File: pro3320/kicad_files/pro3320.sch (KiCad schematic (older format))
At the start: 52 parts

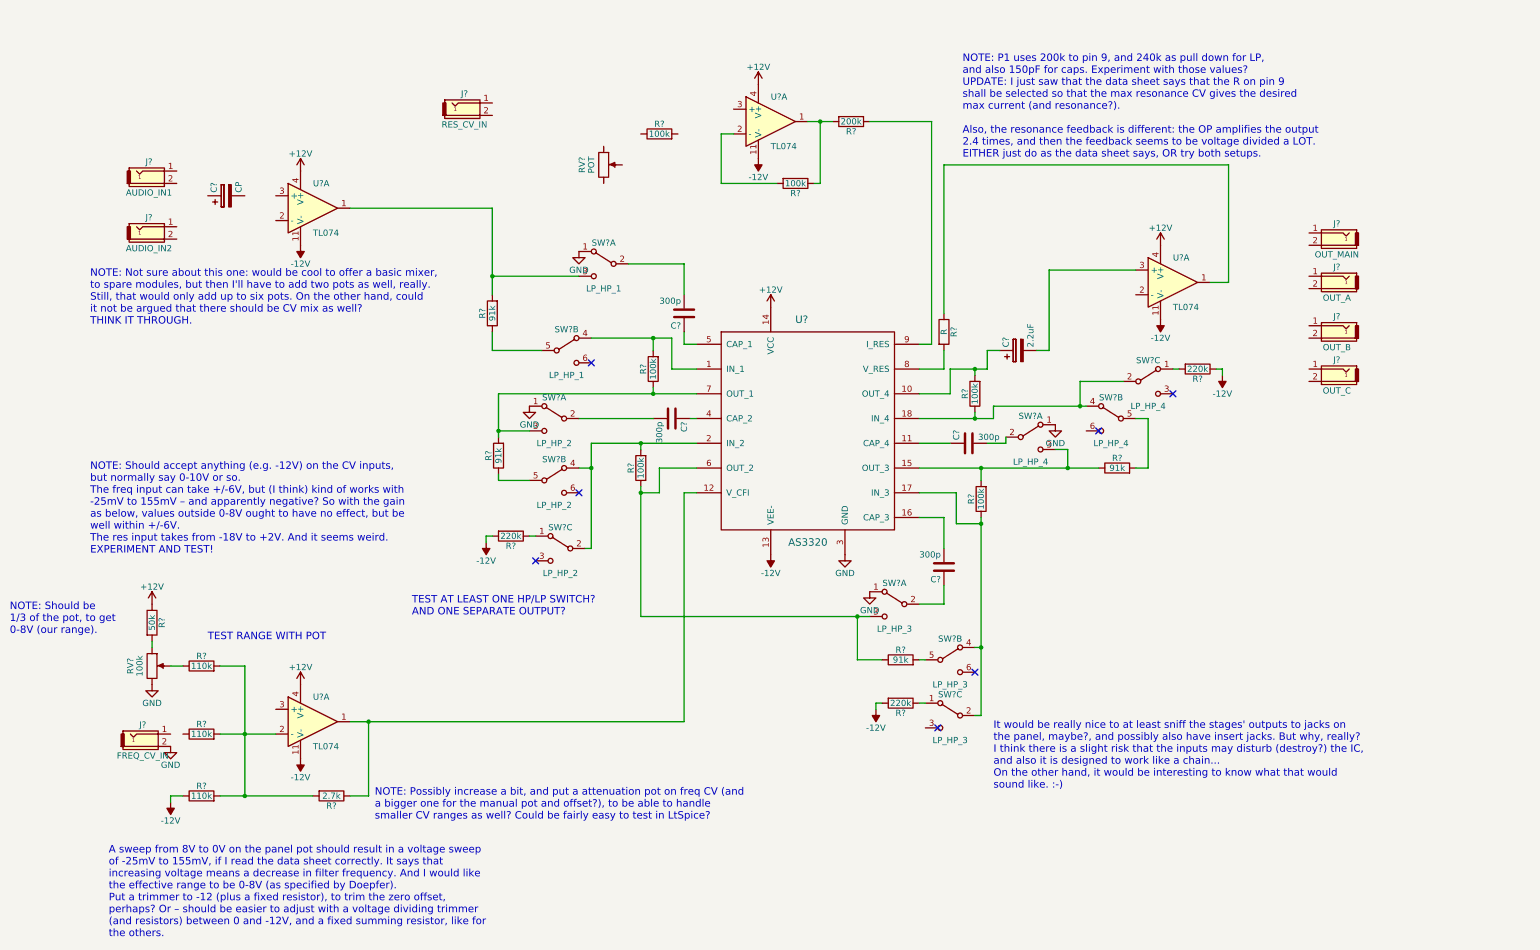
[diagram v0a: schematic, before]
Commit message: Finish (kind of) 3320 VCF
OK, it's not finished as such, nothing is tested at this point.
But the schematic is complete as far as I can tell without having
tested it. :-)
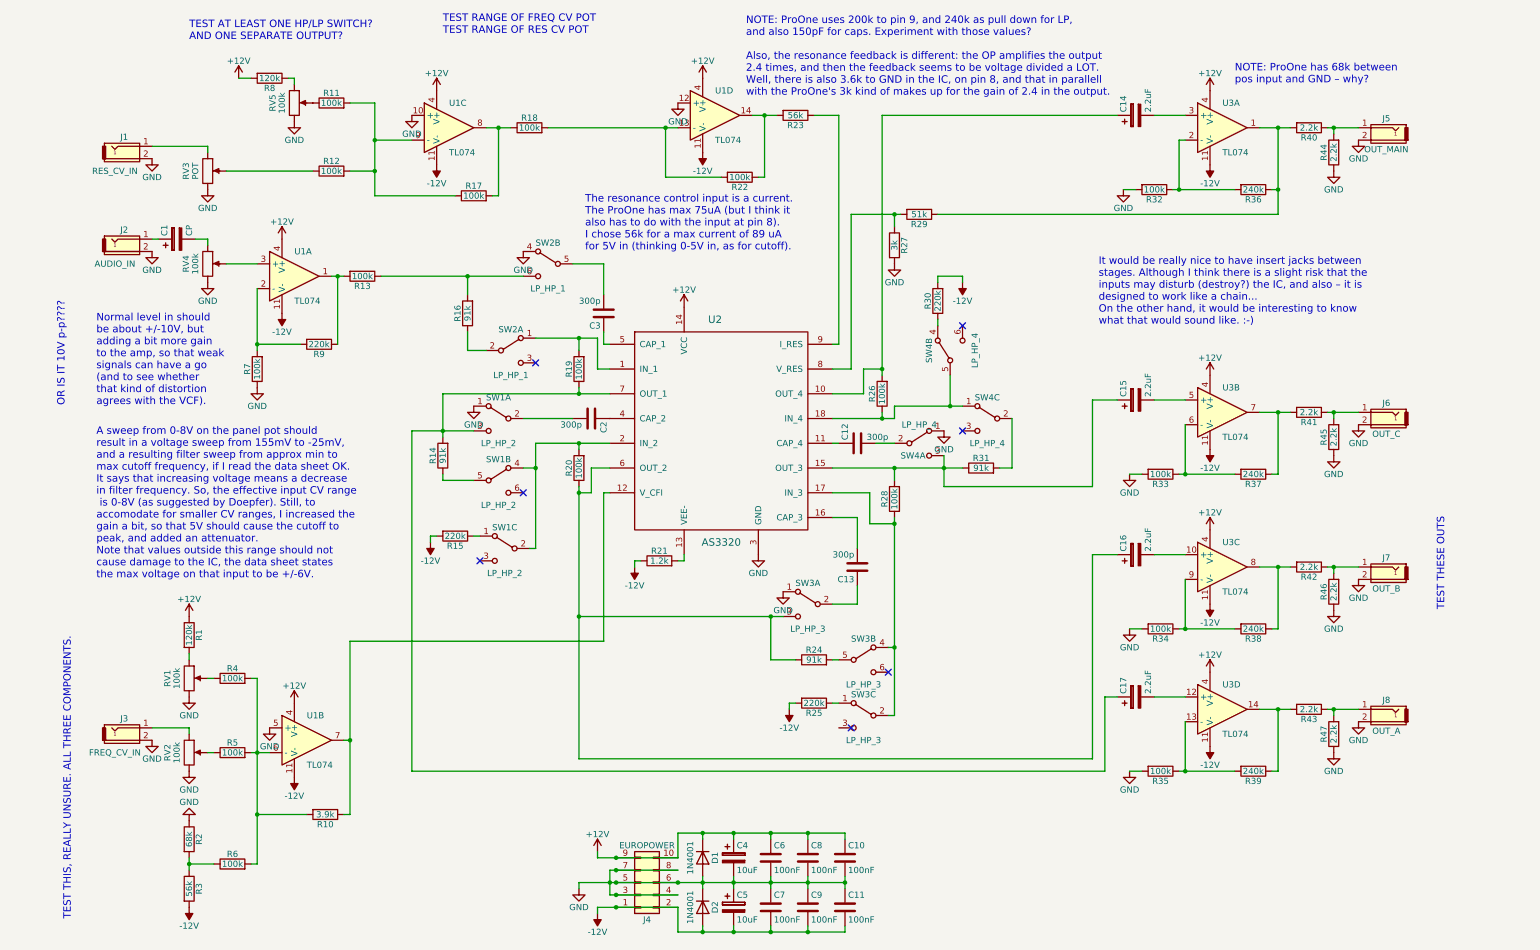
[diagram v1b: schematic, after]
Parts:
- removed J?: AUDIO_IN2, symbol Audio-Jack-2
- added C10, C11, C6, C7, C8, C9: 100nF, symbol C
- added C15, C16, C17: 2.2uF, symbol CP
- added C4, C5: 10uF, symbol CP
- added D1, D2: 1N4001, Diodes_THT:D_DO-41_SOD81_Horizontal_RM10, symbol 1N4001
- added J4: EUROPOWER, symbol Conn_02x05_Odd_Even
- added R11, R12, R13, R18, R32, R33, R34, R35, R7: 100k, symbol R
- added R2: 68k, symbol R
- added R21: 1.2k, symbol R
- added R27: 3k, symbol R
- added R3: 56k, symbol R
- added R36, R37, R38, R39: 240k, symbol R
- added R40, R41, R42, R43, R44, R45, R46, R47: 2.2k, symbol R
- added R8: 120k, symbol R
- added R9: 220k, symbol R
- added RV2, RV4, RV5: 100k, symbol POT
- added unit 3 of U1
- added unit 3 of U3
- added unit 4 of U3
- added unit 2 of U3
- J2: renamed from J?; value AUDIO_IN1 -> AUDIO_IN
- R1: renamed from R?; value 50k -> 120k
- R10: renamed from R?; value 2.7k -> 3.9k
- R23: renamed from R?; value 200k -> 56k
- R29: renamed from R?; value R -> 51k
- R4, R5, R6: renamed from R?; value 110k -> 100k
- gave numbers to parts that had none: 34
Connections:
- net +12V: now also C10.1, C4.1, C6.1, C8.1, D1.1 (K), J4.10 (Pin_10), J4.9 (Pin_9), R8.2, U1.4 (V+), U3.4 (V+), U3.4 (V+), U3.4 (V+)
- net -12V: now also R30.2, C11.2, C5.2, C7.2, C9.2, D2.2 (A), J4.1 (Pin_1), J4.2 (Pin_2), R21.1, R3.2, U1.11 (V-), U3.11 (V-), U3.11 (V-), U3.11 (V-); no longer R30.1, R6.1, U2.13 (VEE-)
- net GND: now also J1.2, J2.2, J5.2, J6.2, J7.2, J8.2, RV3.3, SW2.4 (A), U1.12 (+), U1.5 (+), C10.2, C11.1, C4.2, C5.1, C6.2, C7.1, C8.2, C9.1, D1.2 (A), D2.1 (K), J4.3 (Pin_3), J4.4 (Pin_4), J4.5 (Pin_5), J4.6 (Pin_6), J4.7 (Pin_7), J4.8 (Pin_8), R2.1, R27.2, R32.2, R33.2, R34.2, R35.2, R44.1, R45.1, R46.1, R47.1, R7.1, RV2.3, RV4.3, RV5.3, U1.10 (+); no longer SW2.1 (A)
- net at R19.2, U2.1 (IN_1): now also SW2.1 (A); no longer SW2.4 (A)
- net at R10.1, U2.12 (V_CFI): now also U1.7; no longer U1.1
- net at R28.2, R31.1, SW4.3 (C)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: now also C15.1
- net at R26.1, U2.18 (IN_4): now also SW4.1 (A), SW4.5 (B); no longer SW4.2 (B), SW4.4 (A)
- net at R20.1, R24.1, SW3.3 (C)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: now also C16.1
- net at R14.2, R19.1, SW1.3 (C)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: now also C17.1
- net at R29.2, U2.8 (V_RES): now also R27.1
- net at J3.1: now also RV2.1
- net at J1.1: now also RV3.1
- net at U1.2 (-): now also R7.2, R9.2
- net at U1.3 (+): now also RV4.2
- net at R10.2, R4.2, R5.2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: now also U1.6 (-); no longer U1.2 (-)
- net at R22.1, R23.2: now also U1.14; no longer U1.1
- net at R22.2: now also U1.13 (-), R18.2; no longer U1.2 (-)
- net at R29.1, U3.1: now also R36.1, R40.2
- net at U3.2 (-): now also R32.1, R36.2
- net at J2.1: now also C1.1
- net at C3.2: now also SW2.5 (B); no longer SW2.2 (B)
- net at R16.1: now also SW2.2 (B); no longer SW2.5 (B)
- net at C1.2: now also RV4.1
- net at R31.2: now also SW4.2 (B); no longer SW4.5 (B)
- net at R17.1: now also R11.2, R12.2, U1.9 (-)
- net at R17.2: now also R18.1, U1.8
- net at RV3.2: now also R12.1
- net at R5.1: now also RV2.2
- net at J5.1: now also R40.1, R44.2
- net at J8.1: now also R43.1, R47.2
- net at J7.1: now also R42.1, R46.2
- net at J6.1: now also R41.1, R45.2
- new net: R21.2, U2.13 (VEE-)
- new net: R13.2, R9.1, U1.1
- new net: R13.1, R16.2, SW2.6 (C)
- new net: R30.1, SW4.4 (A)
- new net: R2.2, R3.1, R6.1
- new net: C16.2, U3.10 (+)
- new net: R38.1, R42.2, U3.8
- new net: R34.1, R38.2, U3.9 (-)
- new net: C17.2, U3.12 (+)
- new net: R35.1, R39.2, U3.13 (-)
- new net: R39.1, R43.2, U3.14
- new net: C15.2, U3.5 (+)
- new net: R33.1, R37.2, U3.6 (-)
- new net: R37.1, R41.2, U3.7
- new net: R8.1, RV5.1
- new net: R11.1, RV5.2
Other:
- note added: "A sweep from 0-8V on the panel pot should \nresult in a voltage sweep from 155mV to -25mV, \nand a resulting filter sweep from approx min to \nmax cutoff frequency, if I read the data sheet OK. \nIt says that increasing voltage means a decrease \nin filter frequency. So, the effective input CV range\n is 0-8V (as suggested by Doepfer). Still, to \naccomodate for smaller CV ranges, I increased the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"
- note added: "It would be really nice to have insert jacks between \nstages. Although I think there is a slight risk that the \ninputs may disturb (destroy?) the IC, and also – it is \ndesigned to work like a chain... \nOn the other hand, it would be interesting to know \nwhat that would sound like. :-)"
- note added: "NOTE: ProOne has 68k between \npos input and GND – why?\n"
- note added: "NOTE: ProOne uses 200k to pin 9, and 240k as pull down for LP, \nand also 150pF for caps. Experiment with those values? \n\nAlso, the resonance feedback is different: the OP amplifies the output \n2.4 times, and then the feedback seems to be voltage divided a LOT. \nWell, there is also 3.6k to GND in the IC, on pin 8, and that in parallell\nwith the ProOne's 3k kind of makes up for the gain of 2.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"
- note added: "Normal level in should \nbe about +/-10V, but \nadding a bit more gain \nto the amp, so that weak\nsignals can have a go \n(and to see whether \nthat kind of distortion \nagrees with the VCF)."
- note added: "OR IS IT 10V p-p????\n"
- note added: "TEST RANGE OF FREQ CV POT\nTEST RANGE OF RES CV POT\n"
- note added: "TEST THESE OUTS"
- note added: "TEST THIS, REALLY UNSURE. ALL THREE COMPONENTS."
- note added: "The resonance control input is a current.\nThe ProOne has max 75uA (but I think it\nalso has to do with the input at pin 8).\nI chose 56k for a max current of 89 uA\nfor 5V in (thinking 0-5V in, as for cutoff).\n"
- note removed: "A sweep from 8V to 0V on the panel pot should result in a voltage sweep \nof -25mV to 155mV, if I read the data sheet correctly. It says that \nincreasing voltage means a decrease in filter frequency. And I would like\nthe effective range to be 0-8V (as specified by Doepfer). \nPut a trimmer to -12 (plus a fixed resistor), to trim the zero offset, \nperhaps? Or – should be easier to adjust with a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"
- note removed: "It would be really nice to at least sniff the stages' outputs to jacks on \nthe panel, maybe?, and possibly also have insert jacks. But why, really? \nI think there is a slight risk that the inputs may disturb (destroy?) the IC,\nand also it is designed to work like a chain... \nOn the other hand, it would be interesting to know what that would \nsound like. :-)"
- note removed: "NOTE: Not sure about this one: would be cool to offer a basic mixer,\nto spare modules, but then I'll have to add two pots as well, really. \nStill, that would only add up to six pots. On the other hand, could\nit not be argued that there should be CV mix as well?\nTHINK IT THROUGH."
- note removed: "NOTE: P1 uses 200k to pin 9, and 240k as pull down for LP, \nand also 150pF for caps. Experiment with those values? \nUPDATE: I just saw that the data sheet says that the R on pin 9\nshall be selected so that the max resonance CV gives the desired \nmax current (and resonance?).\n\nAlso, the resonance feedback is different: the OP amplifies the output \n2.4 times, and then the feedback seems to b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"
- note removed: "NOTE: Possibly increase a bit, and put a attenuation pot on freq CV (and \na bigger one for the manual pot and offset?), to be able to handle \nsmaller CV ranges as well? Could be fairly easy to test in LtSpice?"
- note removed: "NOTE: Should accept anything (e.g. -12V) on the CV inputs, \nbut normally say 0-10V or so. \nThe freq input can take +/-6V, but (I think) kind of works with \n-25mV to 155mV – and apparently negative? So with the gain\nas below, values outside 0-8V ought to have no effect, but be \nwell within +/-6V.\nThe res input takes from -18V to +2V. And it seems weird. \nEXPERIMENT AND TEST!"
- note removed: "NOTE: Should be\n1/3 of the pot, to get\n0-8V (our range)."
- note removed: "TEST RANGE WITH POT\n"
- moved on the sheet: C1, C12, C13, C14, C2, C3, J1, J2, J3, J5, J6, J7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
